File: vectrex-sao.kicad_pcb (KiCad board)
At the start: 2 copper layers, 46.8 x 62 mm, 104 parts, among them J1 ICSP, J2 SAO_v169bis, Q1 MMBT3904, U1 PIC16F886-IP, U2 IS31FL3731-SALS2, U3 TC233A

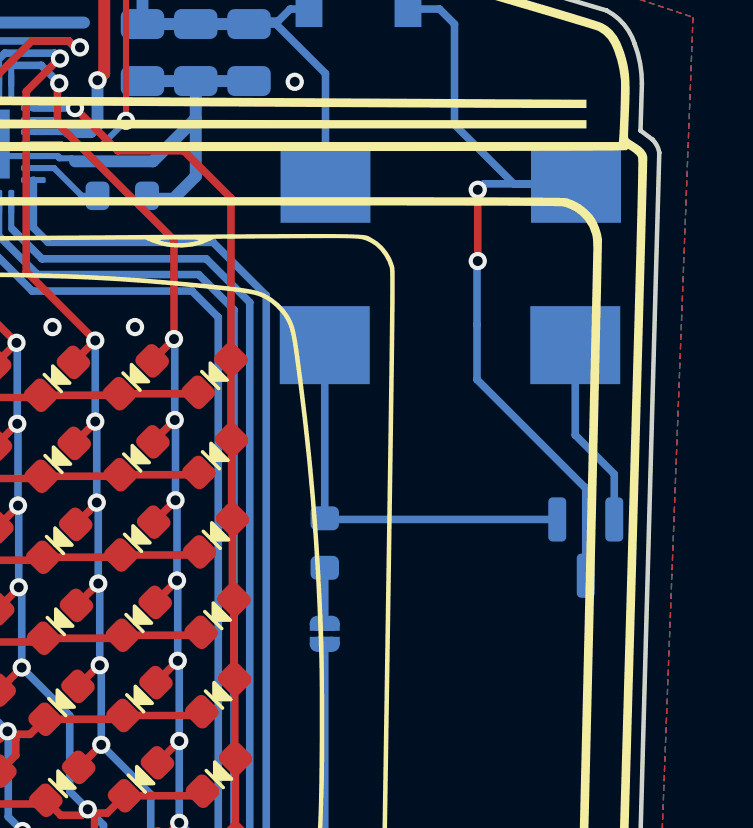
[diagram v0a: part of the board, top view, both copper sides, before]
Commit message: update files for easier mass production with JLCPCB
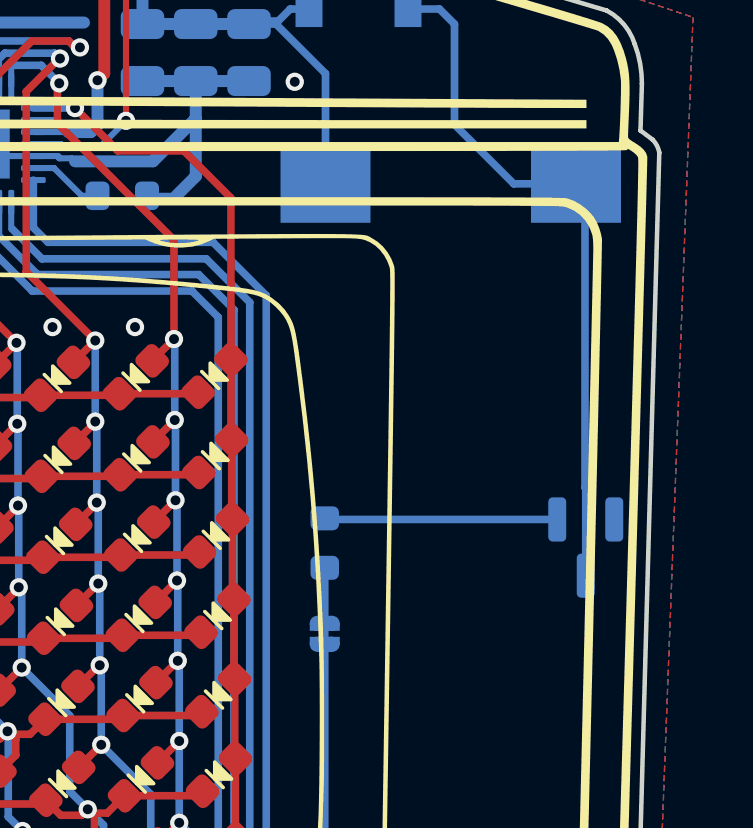
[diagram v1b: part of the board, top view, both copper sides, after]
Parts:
- removed LS2: Speaker FUET-9032-05, vectrex-sao:MagneticBuzzer_FUET-9032-05
- JP9: footprint vectrex-sao:SolderJumper-2_P1.3mm_Open_RoundedPad1.0x1.5mm -> vectrex-sao:SolderJumper-2_P1.3mm_Bridged_RoundedPad1.0x1.5mm
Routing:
- net GND: track 143.7 -> 136.7 mm
- net Net-(Q1-B): track 13.5 -> 7.77 mm
- net Net-(D1-A): track 27.7 -> 23.2 mm, vias 2 -> 0
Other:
- board text added: "Vectrex SAO - Supercon '25"
- board text removed: "Vectrex SAO - Supercon '22"
